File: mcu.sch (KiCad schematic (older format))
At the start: 53 parts, among them P11 CONN_01X01, P16 CONN_01X01, P17 CONN_01X01, P21 CONN_01X01, P22 CONN_01X01, P23 CONN_01X01, P28 CONN_01X01, P29 CONN_01X01, P3 CONN_01X05, P30 CONN_01X01, P32 CONN_01X01, P33 CONN_01X01, P34 CONN_01X01, P35 CONN_01X01, P36 CONN_01X01, P37 CONN_01X01, P4 CONN_01X04, P5 CONN_01X01, P6 CONN_01X01, P9 CONN_01X01, Y1 ABMM2-8.000MHZ-E2-T

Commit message: Stand 10.03
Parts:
- removed C37, C38: 18p, Capacitors_SMD:C_0603, symbol C_Small
- removed C40, C41: 1u, Capacitors_SMD:C_0603, symbol C_Small
- removed C44: 47u, Capacitors_SMD:C_0805, symbol C_Small
- removed C95: 100n, Capacitors_SMD:C_0603, symbol C_Small
- removed C960: 10u, Capacitors_SMD:C_0603, symbol C_Small
- removed D14: BAT54SW, TO_SOT_Packages_SMD:SOT-323, symbol BAT54SW
- removed Y1: ABMM2-8.000MHZ-E2-T, Crystals:Crystal_SMD_5032_4Pads, symbol Crystal_Small
- added C? (x2): 18p, symbol C_Small
- added P?: CONN_01X04, Connectors_Molex:Molex_KK-6410-04_04x2.54mm_Straight, symbol CONN_01X04
- added P? (x3): CONN_01X01, Connect:PINTST, symbol CONN_01X01
- added R? (x2): 10k, symbol R_Small
- added Y?: ABMM2-8.000MHZ-E2-T, Crystals:Crystal_SMD_5032-4pin_5.0x3.2mm, symbol Crystal_Small
- U?: value MKE14F256_v.1.1 -> MKE14F256_v.1.2; footprint (none) -> Housings_QFP:LQFP-64_10x10mm_Pitch0.5mm; symbol MKE14F256_v.1.1 -> MKE14F256_v.1.3
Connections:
- net labels added: DC_3V6, DC_Vin, PWM_HS, PWM_LS, led_blu
- net labels removed: ADC_CH_SEL, ADC_DVDD, PWM_HS_1, PWM_HS_2, PWM_HS_3, PWM_HS_4, PWM_LS_1, PWM_LS_2, PWM_LS_3, PWM_LS_4, Sense_Curr_1, Sense_Curr_2, Sense_Curr_3, Sense_Curr_4, Sense_Inp_Volt, Sense_Out_Volt_1, Sense_Out_Volt_2, Sense_Out_Volt_3, Sense_Out_Volt_4, VREFH, V_12V, led_ble
- wire segments 154 -> 131
- no-connect marks 5 -> 2
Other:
- moved on the sheet: P11, P16, P17, P21, P22, P23, P28, P29, P30, P9

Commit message: schematics ==> Check (exept BW) Layout started
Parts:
- added C37: 10n, Capacitors_SMD:C_0603, symbol C_Small
- C27, C28, C29, C30, C31, C32, C36: renamed from C?; footprint (none) -> Capacitors_SMD:C_0603
- C34: renamed from C?; value 100n -> 1n; footprint (none) -> Capacitors_SMD:C_0603
- D7: renamed from D15; footprint TO_SOT_Packages_SMD:SOT-323 -> TO_SOT_Packages_SMD:SOT-323_SC-70
- D8: renamed from D16; footprint TO_SOT_Packages_SMD:SOT-323 -> TO_SOT_Packages_SMD:SOT-323_SC-70
- R23, R24, R28: renamed from R?; footprint (none) -> Resistors_SMD:R_0603
- R25: renamed from R?; value 10k -> 47k; footprint (none) -> Resistors_SMD:R_0603
- XS1: renamed from XS?; footprint Connectors:Conn_uSDcard -> .pretty:uSDcard
- gave numbers to parts that had none: 6
- renumbered C501 to C33, C500 to C35, D5 to D3, D11 to D4, D13 to D5, D30 to D6, P30 to P10, P16 to P11, P11 to P12, P17 to P13, P21 to P14, P22 to P16, P23 to P17, P5 to P20, P6 to P21, P32 to P22, P33 to P23, P34 to P24, P35 to P25, P36 to P26, P37 to P27, P3 to P5, P4 to P6, P9 to P7, P28 to P8, P29 to P9, R36 to R19, R37 to R20, R38 to R21, R39 to R22, R49 to R26, R50 to R27
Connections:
- net GND: now also C37.1
- net Vref: now also C37.2
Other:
- moved on the sheet: C34

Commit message: changed usd slot
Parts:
- XS1: footprint .pretty:uSDcard -> .pretty:HIROSE-MICROSD-DM3AT-SF
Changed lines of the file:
@@
 F 0 "XS1" H 6330 9780 50  0000 C CNN
 F 1 "SD_ebay-uSD-push/push_SMD" V 5780 10355 50  0000 C CNN
-F 2 ".pretty:uSDcard" H 6105 10355 10  0001 C CNN
+F 2 ".pretty:HIROSE-MICROSD-DM3AT-SF" H 6105 10355 10  0001 C CNN
 F 3 "_" H 6105 10355 10  0001 C CNN
 F 4 "_" H 6105 10355 10  0001 C CNN "Manf#"

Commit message: All parts in places (exept :Leds)
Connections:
- net ADC_1: now also U7.52 (PTC6); no longer U7.51 (PTC7)
- net ADC_2: now also U7.54 (PTE2); no longer U7.52 (PTC6)
- net ADC_3: now also U7.51 (PTC7); no longer U7.53 (PTE6)
- net ADC_4: now also U7.53 (PTE6); no longer U7.54 (PTE2)
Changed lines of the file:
@@
 ADC_PDEN
 Text GLabel 10960 3460 2    39   Input ~ 0
+ADC_3
+Text GLabel 10960 3610 2    39   Input ~ 0
 ADC_1
-Text GLabel 10960 3610 2    39   Input ~ 0
+Text GLabel 10960 3760 2    39   Input ~ 0
+ADC_4
+Text GLabel 10960 3910 2    39   Input ~ 0
 ADC_2
-Text GLabel 10960 3760 2    39   Input ~ 0
-ADC_3
-Text GLabel 10960 3910 2    39   Input ~ 0
-ADC_4
 Text GLabel 3780 6060 0    60   Input ~ 0
 Boost_Enable

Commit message: Started with tracking
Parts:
- Y1: symbol Crystal_Small -> QUARTZCMS4
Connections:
- net at C28.1, U7.12 (PTB6): now also Y1.3; no longer Y1.2
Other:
- moved on the sheet: C27, C28
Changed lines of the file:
@@
 L C_Small C28
 U 1 1 58C580AB
-P 3455 7285
-F 0 "C28" H 3465 7355 50  0000 L CNN
-F 1 "18p" H 3465 7205 50  0000 L CNN
-F 2 "Capacitors_SMD:C_0603" H 3455 7285 50  0001 C CNN
-F 3 "" H 3455 7285 50  0000 C CNN
-	1    3455 7285
+P 3455 7210
+F 0 "C28" H 3465 7280 50  0000 L CNN
+F 1 "18p" H 3465 7130 50  0000 L CNN
+F 2 "Capacitors_SMD:C_0603" H 3455 7210 50  0001 C CNN
+F 3 "" H 3455 7210 50  0000 C CNN
+	1    3455 7210
 	1    0    0    -1
 $EndComp
@@
 L C_Small C27
 U 1 1 58C58C12
-P 3105 7280
-F 0 "C27" H 3115 7350 50  0000 L CNN
-F 1 "18p" H 3115 7200 50  0000 L CNN
-F 2 "Capacitors_SMD:C_0603" H 3105 7280 50  0001 C CNN
-F 3 "" H 3105 7280 50  0000 C CNN
-	1    3105 7280
-	1    0    0    -1
-$EndComp
-$Comp
-L Crystal_Small Y1
+P 2850 7200
+F 0 "C27" H 2860 7270 50  0000 L CNN
+F 1 "18p" H 2860 7120 50  0000 L CNN
+F 2 "Capacitors_SMD:C_0603" H 2850 7200 50  0001 C CNN
+F 3 "" H 2850 7200 50  0000 C CNN
+	1    2850 7200
+	1    0    0    -1
+$EndComp
+$Comp
+L QUARTZCMS4 Y1
 U 1 1 58C5C5B8
-P 3295 7045
-F 0 "Y1" H 3295 7145 50  0000 C CNN
-F 1 "ABMM2-8.000MHZ-E2-T" H 2600 7135 50  0000 C CNN
-F 2 "Crystals:Crystal_SMD_5032-4pin_5.0x3.2mm" H 3295 7045 50  0001 C CNN
-F 3 "http://www.mouser.com/ds/2/3/ABMM2-40161.pdf" H 3295 7045 50  0001 C CNN
-F 4 "815-ABMM2-8-E2T" H 3295 7045 60  0001 C CNN "Mouser"
-	1    3295 7045
+P 3150 7015
+F 0 "Y1" H 3150 7115 50  0000 C CNN
+F 1 "ABMM2-8.000MHZ-E2-T" H 2455 7105 50  0000 C CNN
+F 2 "Crystals:Crystal_SMD_5032-4pin_5.0x3.2mm" H 3150 7015 50  0001 C CNN
+F 3 "http://www.mouser.com/ds/2/3/ABMM2-40161.pdf" H 3150 7015 50  0001 C CNN
+F 4 "815-ABMM2-8-E2T" H 3150 7015 60  0001 C CNN "Mouser"
+	1    3150 7015
 	1    0    0    -1
 $EndComp
@@
 L GND #PWR075
 U 1 1 58C5EAC8
-P 3105 7415
-F 0 "#PWR075" H 3105 7165 50  0001 C CNN
-F 1 "GND" H 3105 7265 50  0000 C CNN
-F 2 "" H 3105 7415 50  0000 C CNN
-F 3 "" H 3105 7415 50  0000 C CNN
-	1    3105 7415
+P 2850 7340
+F 0 "#PWR075" H 2850 7090 50  0001 C CNN
+F 1 "GND" H 2850 7190 50  0000 C CNN
+F 2 "" H 2850 7340 50  0000 C CNN
+F 3 "" H 2850 7340 50  0000 C CNN
+	1    2850 7340
 	1    0    0    -1
 $EndComp
@@
 L GND #PWR076
 U 1 1 58C5F3E4
-P 3455 7415
-F 0 "#PWR076" H 3455 7165 50  0001 C CNN
-F 1 "GND" H 3455 7265 50  0000 C CNN
-F 2 "" H 3455 7415 50  0000 C CNN
-F 3 "" H 3455 7415 50  0000 C CNN
-	1    3455 7415
+P 3455 7340
+F 0 "#PWR076" H 3455 7090 50  0001 C CNN
+F 1 "GND" H 3455 7190 50  0000 C CNN
+F 2 "" H 3455 7340 50  0000 C CNN
+F 3 "" H 3455 7340 50  0000 C CNN
+	1    3455 7340
 	1    0    0    -1
 $EndComp
@@
 Wire Wire Line
 	10960 3910 10825 3910
-Connection ~ 3105 7045
-Wire Wire Line
-	3925 6710 3105 6710
-Connection ~ 3455 7045
+Wire Wire Line
+	2850 6710 3925 6710
 Wire Wire Line
 	3925 6860 3455 6860
 Wire Wire Line
-	3455 7415 3455 7385
-Wire Wire Line
-	3105 7415 3105 7380
-Wire Wire Line
-	3105 6710 3105 7180
-Wire Wire Line
-	3195 7045 3105 7045
-Wire Wire Line
-	3455 7045 3395 7045
-Wire Wire Line
-	3455 6860 3455 7185
+	3455 7340 3455 7310
+Wire Wire Line
+	2850 7340 2850 7300
 Wire Wire Line
 	11070 6210 10825 6210
@@
 $EndComp
 Wire Wire Line
-	8990 1970 8740 1970
+	8740 1970 8990 1970
 Connection ~ 8875 1970
 Wire Wire Line
@@
 	8945 2135 8945 1970
 Connection ~ 8945 1970
+Wire Wire Line
+	3455 6860 3455 7110
+Wire Wire Line
+	3455 7015 3450 7015
+Connection ~ 3455 7015
+Wire Wire Line
+	2850 6710 2850 7100
+Connection ~ 2850 7015
 $EndSCHEMATC

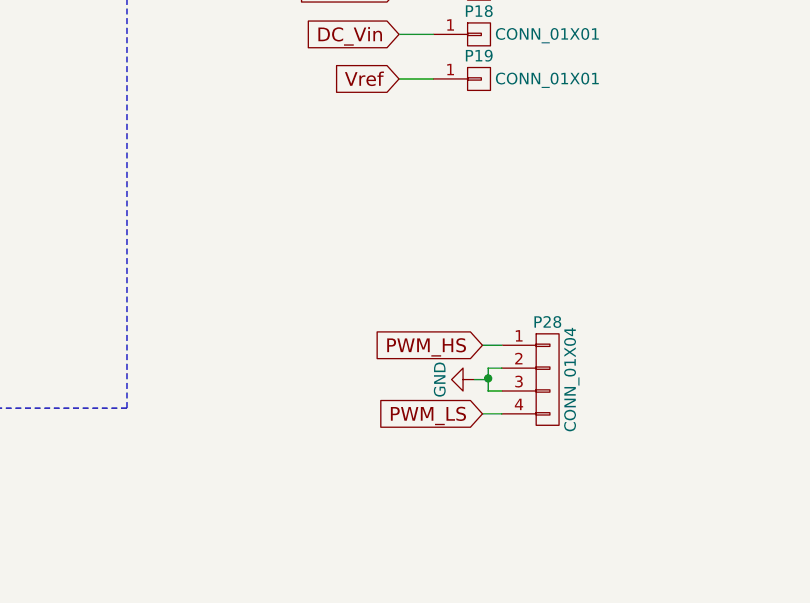
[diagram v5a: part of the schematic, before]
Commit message: added missing parts (SPI conn / Boost Conn/ drills..)
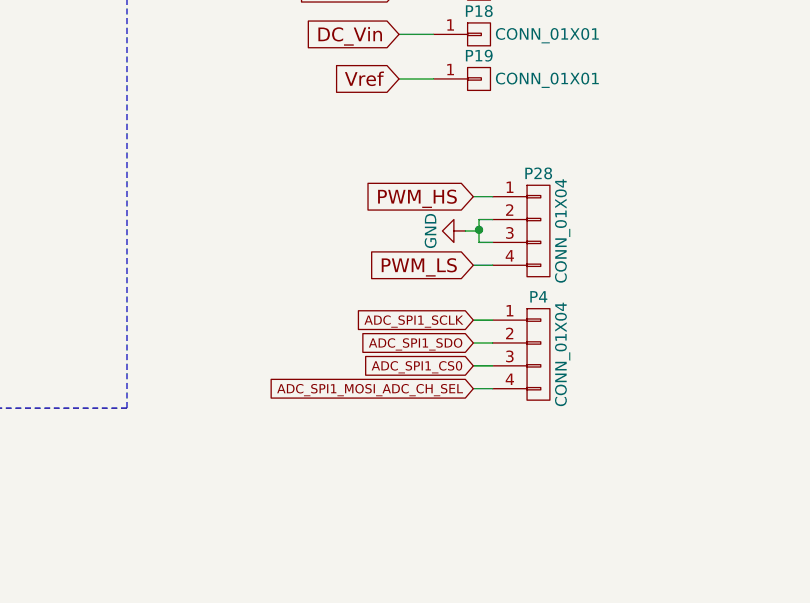
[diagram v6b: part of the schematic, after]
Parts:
- added P4: CONN_01X04, Connectors_Molex:Molex_KK-6410-04_04x2.54mm_Straight, symbol CONN_01X04
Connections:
- net ADC_SPI1_CS0: now also P4.3 (P3)
- net ADC_SPI1_MOSI_ADC_CH_SEL: now also P4.4 (P4)
- net ADC_SPI1_SCLK: now also P4.1 (P1)
- net ADC_SPI1_SDO: now also P4.2 (P2)
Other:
- moved on the sheet: P28

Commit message: still the regulators & Planes fill
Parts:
- U7: symbol MKE14F256_v.1.3 -> MKE14F256_v.1.4
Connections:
- net ADC_PDEN: now also U7.26 (PTC0); no longer U7.43 (PTB12)
- net led_blu: now also U7.47 (PTA3); no longer U7.28 (PTC16)
- net led_grn: now also U7.49 (PTA1); no longer U7.27 (PTC17)
- net led_red: now also U7.48 (PTA2); no longer U7.25 (PTC1)
- net led_yel: now also U7.50 (PTA0); no longer U7.26 (PTC0)
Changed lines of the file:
@@
 $EndComp
 $Comp
-L +3.3V #PWR71
+L +3.3V #PWR046
 U 1 1 57321F1B
 P 10876 9751
-F 0 "#PWR71" H 10876 9601 50  0001 C CNN
+F 0 "#PWR046" H 10876 9601 50  0001 C CNN
 F 1 "+3.3V" H 10876 9891 50  0000 C CNN
 F 2 "" H 10876 9751 50  0000 C CNN
@@
 $EndComp
 $Comp
-L GND #PWR72
+L GND #PWR047
 U 1 1 573220D0
 P 10876 10251
-F 0 "#PWR72" H 10876 10001 50  0001 C CNN
+F 0 "#PWR047" H 10876 10001 50  0001 C CNN
 F 1 "GND" H 10876 10101 50  0000 C CNN
 F 2 "" H 10876 10251 50  0000 C CNN
@@
 $EndComp
 $Comp
-L GND #PWR70
+L GND #PWR048
 U 1 1 57323943
 P 10176 10501
-F 0 "#PWR70" H 10176 10251 50  0001 C CNN
+F 0 "#PWR048" H 10176 10251 50  0001 C CNN
 F 1 "GND" H 10176 10351 50  0000 C CNN
 F 2 "" H 10176 10501 50  0000 C CNN
@@
 $EndComp
 $Comp
-L +3.3V #PWR64
+L +3.3V #PWR049
 U 1 1 57323984
 P 8976 10451
-F 0 "#PWR64" H 8976 10301 50  0001 C CNN
+F 0 "#PWR049" H 8976 10301 50  0001 C CNN
 F 1 "+3.3V" H 8976 10591 50  0000 C CNN
 F 2 "" H 8976 10451 50  0000 C CNN
@@
 $EndComp
 $Comp
-L +3.3V #PWR68
+L +3.3V #PWR050
 U 1 1 573239C5
 P 9626 10451
-F 0 "#PWR68" H 9626 10301 50  0001 C CNN
+F 0 "#PWR050" H 9626 10301 50  0001 C CNN
 F 1 "+3.3V" H 9626 10591 50  0000 C CNN
 F 2 "" H 9626 10451 50  0000 C CNN
@@
 $EndComp
 $Comp
-L GND #PWR67
+L GND #PWR051
 U 1 1 57323B3B
 P 9476 10501
-F 0 "#PWR67" H 9476 10251 50  0001 C CNN
+F 0 "#PWR051" H 9476 10251 50  0001 C CNN
 F 1 "GND" H 9476 10351 50  0000 C CNN
 F 2 "" H 9476 10501 50  0000 C CNN
@@
 $EndComp
 $Comp
-L +3.3V #PWR55
+L +3.3V #PWR052
 U 1 1 57346289
 P 4291 9953
-F 0 "#PWR55" H 4291 9803 50  0001 C CNN
+F 0 "#PWR052" H 4291 9803 50  0001 C CNN
 F 1 "+3.3V" H 4291 10093 50  0000 C CNN
 F 2 "" H 4291 9953 50  0000 C CNN
@@
 $EndComp
 $Comp
-L GND #PWR54
+L GND #PWR053
 U 1 1 57346821
 P 4241 10453
-F 0 "#PWR54" H 4241 10203 50  0001 C CNN
+F 0 "#PWR053" H 4241 10203 50  0001 C CNN
 F 1 "GND" H 4241 10303 50  0000 C CNN
 F 2 "" H 4241 10453 50  0000 C CNN
@@
 ADC_1
 $Comp
-L +3.3V #PWR75
+L +3.3V #PWR054
 U 1 1 57613741
 P 14935 5810
-F 0 "#PWR75" H 14935 5660 50  0001 C CNN
+F 0 "#PWR054" H 14935 5660 50  0001 C CNN
 F 1 "+3.3V" H 14935 5950 50  0000 C CNN
 F 2 "" H 14935 5810 50  0000 C CNN
@@
 $EndComp
 $Comp
-L GND #PWR77
+L GND #PWR055
 U 1 1 57613EB7
 P 14935 6310
-F 0 "#PWR77" H 14935 6060 50  0001 C CNN
+F 0 "#PWR055" H 14935 6060 50  0001 C CNN
 F 1 "GND" H 14935 6160 50  0000 C CNN
 F 2 "" H 14935 6310 50  0000 C CNN
@@
 $EndComp
 $Comp
-L GND #PWR78
+L GND #PWR056
 U 1 1 57614C38
 P 14935 6560
-F 0 "#PWR78" H 14935 6310 50  0001 C CNN
+F 0 "#PWR056" H 14935 6310 50  0001 C CNN
 F 1 "GND" H 14935 6410 50  0000 C CNN
 F 2 "" H 14935 6560 50  0000 C CNN
@@
 $EndComp
 $Comp
-L +3.3V #PWR80
+L +3.3V #PWR057
 U 1 1 57618324
 P 14940 6965
-F 0 "#PWR80" H 14940 6815 50  0001 C CNN
+F 0 "#PWR057" H 14940 6815 50  0001 C CNN
 F 1 "+3.3V" H 14940 7105 50  0000 C CNN
 F 2 "" H 14940 6965 50  0000 C CNN
@@
 $EndComp
 $Comp
-L GND #PWR46
+L GND #PWR058
 U 1 1 576344D4
 P 1622 10663
-F 0 "#PWR46" H 1622 10413 50  0001 C CNN
+F 0 "#PWR058" H 1622 10413 50  0001 C CNN
 F 1 "GND" H 1622 10513 50  0000 C CNN
 F 2 "" H 1622 10663 50  0000 C CNN
@@
 $EndComp
 $Comp
-L GND #PWR47
+L GND #PWR059
 U 1 1 57634A1E
 P 1972 10663
-F 0 "#PWR47" H 1972 10413 50  0001 C CNN
+F 0 "#PWR059" H 1972 10413 50  0001 C CNN
 F 1 "GND" H 1972 10513 50  0000 C CNN
 F 2 "" H 1972 10663 50  0000 C CNN
@@
 $EndComp
 $Comp
-L GND #PWR48
+L GND #PWR060
 U 1 1 57634A8E
 P 2272 10663
-F 0 "#PWR48" H 2272 10413 50  0001 C CNN
+F 0 "#PWR060" H 2272 10413 50  0001 C CNN
 F 1 "GND" H 2272 10513 50  0000 C CNN
 F 2 "" H 2272 10663 50  0000 C CNN
@@
 $EndComp
 $Comp
-L GND #PWR49
+L GND #PWR061
 U 1 1 57634AFE
 P 2572 10663
-F 0 "#PWR49" H 2572 10413 50  0001 C CNN
+F 0 "#PWR061" H 2572 10413 50  0001 C CNN
 F 1 "GND" H 2572 10513 50  0000 C CNN
 F 2 "" H 2572 10663 50  0000 C CNN
@@
 CMP1_IN1_Overvoltage_Prot
 $Comp
-L GND #PWR76
+L GND #PWR062
 U 1 1 57C00D54
 P 14935 6060
-F 0 "#PWR76" H 14935 5810 50  0001 C CNN
+F 0 "#PWR062" H 14935 5810 50  0001 C CNN
 F 1 "GND" H 14935 5910 50  0000 C CNN
 F 2 "" H 14935 6060 50  0000 C CNN
@@
 $EndComp
 $Comp
-L GND #PWR69
+L GND #PWR063
 U 1 1 57C35C43
 P 9656 10791
-F 0 "#PWR69" H 9656 10541 50  0001 C CNN
+F 0 "#PWR063" H 9656 10541 50  0001 C CNN
 F 1 "GND" H 9656 10641 50  0000 C CNN
 F 2 "" H 9656 10791 50  0000 C CNN
@@
 $EndComp
 $Comp
-L GND #PWR65
+L GND #PWR064
 U 1 1 57C35CF6
 P 9006 10791
-F 0 "#PWR65" H 9006 10541 50  0001 C CNN
+F 0 "#PWR064" H 9006 10541 50  0001 C CNN
 F 1 "GND" H 9006 10641 50  0000 C CNN
 F 2 "" H 9006 10791 50  0000 C CNN
@@
 $EndComp
 $Comp
-L +3.3V #PWR56
+L +3.3V #PWR065
 U 1 1 58BE06E5
 P 5955 9380
-F 0 "#PWR56" H 5955 9230 50  0001 C CNN
+F 0 "#PWR065" H 5955 9230 50  0001 C CNN
 F 1 "+3.3V" H 5955 9520 50  0000 C CNN
 F 2 "" H 5955 9380 50  0000 C CNN
@@
 $EndComp
 $Comp
-L GND #PWR58
+L GND #PWR066
 U 1 1 58BE131B
 P 6240 9645
-F 0 "#PWR58" H 6240 9395 50  0001 C CNN
+F 0 "#PWR066" H 6240 9395 50  0001 C CNN
 F 1 "GND" H 6240 9495 50  0000 C CNN
 F 2 "" H 6240 9645 50  0000 C CNN
@@
 $EndComp
 $Comp
-L GND #PWR57
+L GND #PWR067
 U 1 1 58BE2C3C
 P 5955 11020
-F 0 "#PWR57" H 5955 10770 50  0001 C CNN
+F 0 "#PWR067" H 5955 10770 50  0001 C CNN
 F 1 "GND" H 5955 10870 50  0000 C CNN
 F 2 "" H 5955 11020 50  0000 C CNN
@@
 Text GLabel 11070 6060 2    60   Input ~ 0
 ADC_SPI1_CS0
-Text GLabel 11060 2560 2    60   Input ~ 0
+Text GLabel 3690 3410 0    60   Input ~ 0
 ADC_PDEN
 Text GLabel 10960 3460 2    39   Input ~ 0
@@
 Vref
 $Comp
-L +3.3V #PWR61
+L +3.3V #PWR068
 U 1 1 58C38171
 P 8075 1195
-F 0 "#PWR61" H 8075 1045 50  0001 C CNN
+F 0 "#PWR068" H 8075 1045 50  0001 C CNN
 F 1 "+3.3V" H 8075 1335 50  0000 C CNN
 F 2 "" H 8075 1195 50  0000 C CNN
@@
 $EndComp
 $Comp
-L +3.3V #PWR62
+L +3.3V #PWR069
 U 1 1 58C38898
 P 8275 1190
-F 0 "#PWR62" H 8275 1040 50  0001 C CNN
+F 0 "#PWR069" H 8275 1040 50  0001 C CNN
 F 1 "+3.3V" H 8275 1330 50  0000 C CNN
 F 2 "" H 8275 1190 50  0000 C CNN
@@
 $EndComp
 $Comp
-L +3.3V #PWR63
+L +3.3V #PWR070
 U 1 1 58C38936
 P 8475 1190
-F 0 "#PWR63" H 8475 1040 50  0001 C CNN
+F 0 "#PWR070" H 8475 1040 50  0001 C CNN
 F 1 "+3.3V" H 8475 1330 50  0000 C CNN
 F 2 "" H 8475 1190 50  0000 C CNN
@@
 $EndComp
 $Comp
-L GND #PWR66
+L GND #PWR071
 U 1 1 58C3DCC7
 P 9365 2030
-F 0 "#PWR66" H 9365 1780 50  0001 C CNN
+F 0 "#PWR071" H 9365 1780 50  0001 C CNN
 F 1 "GND" H 9365 1880 50  0000 C CNN
 F 2 "" H 9365 2030 50  0000 C CNN
@@
 $EndComp
 $Comp
-L GND #PWR60
+L GND #PWR072
 U 1 1 58C4F8DB
 P 6475 7740
-F 0 "#PWR60" H 6475 7490 50  0001 C CNN
+F 0 "#PWR072" H 6475 7490 50  0001 C CNN
 F 1 "GND" H 6475 7590 50  0000 C CNN
 F 2 "" H 6475 7740 50  0000 C CNN
@@
 $EndComp
 $Comp
-L GND #PWR59
+L GND #PWR073
 U 1 1 58C4FCDC
 P 6275 7740
-F 0 "#PWR59" H 6275 7490 50  0001 C CNN
+F 0 "#PWR073" H 6275 7490 50  0001 C CNN
 F 1 "GND" H 6275 7590 50  0000 C CNN
 F 2 "" H 6275 7740 50  0000 C CNN
@@
 $EndComp
 $Comp
-L +3.3V #PWR74
+L +3.3V #PWR074
 U 1 1 58C66D72
 P 11680 7160
-F 0 "#PWR74" H 11680 7010 50  0001 C CNN
+F 0 "#PWR074" H 11680 7010 50  0001 C CNN
 F 1 "+3.3V" H 11680 7300 50  0000 C CNN
 F 2 "" H 11680 7160 50  0000 C CNN
@@
 $EndComp
 $Comp
-L GND #PWR73
+L GND #PWR075
 U 1 1 58C68B69
 P 11240 7505
-F 0 "#PWR73" H 11240 7255 50  0001 C CNN
+F 0 "#PWR075" H 11240 7255 50  0001 C CNN
 F 1 "GND" H 11240 7355 50  0000 C CNN
 F 2 "" H 11240 7505 50  0000 C CNN
@@
 $EndComp
 $Comp
-L GND #PWR50
+L GND #PWR076
 U 1 1 58C5EAC8
 P 2850 7340
-F 0 "#PWR50" H 2850 7090 50  0001 C CNN
+F 0 "#PWR076" H 2850 7090 50  0001 C CNN
 F 1 "GND" H 2850 7190 50  0000 C CNN
 F 2 "" H 2850 7340 50  0000 C CNN
@@
 $EndComp
 $Comp
-L GND #PWR51
+L GND #PWR077
 U 1 1 58C5F3E4
 P 3455 7340
-F 0 "#PWR51" H 3455 7090 50  0001 C CNN
+F 0 "#PWR077" H 3455 7090 50  0001 C CNN
 F 1 "GND" H 3455 7190 50  0000 C CNN
 F 2 "" H 3455 7340 50  0000 C CNN
@@
 $EndComp
 $Comp
-L GND #PWR52
+L GND #PWR078
 U 1 1 58C97D80
 P 3465 2975
-F 0 "#PWR52" H 3465 2725 50  0001 C CNN
+F 0 "#PWR078" H 3465 2725 50  0001 C CNN
 F 1 "GND" H 3465 2825 50  0000 C CNN
 F 2 "" H 3465 2975 50  0000 C CNN
@@
 $EndComp
 $Comp
-L GND #PWR53
+L GND #PWR079
 U 1 1 58C9831F
 P 3675 2975
-F 0 "#PWR53" H 3675 2725 50  0001 C CNN
+F 0 "#PWR079" H 3675 2725 50  0001 C CNN
 F 1 "GND" H 3675 2825 50  0000 C CNN
 F 2 "" H 3675 2975 50  0000 C CNN
@@
 	15250 8375 15165 8375
 $Comp
-L GND #PWR81
+L GND #PWR080
 U 1 1 58CA8BCD
 P 15130 8225
-F 0 "#PWR81" H 15130 7975 50  0001 C CNN
+F 0 "#PWR080" H 15130 7975 50  0001 C CNN
 F 1 "GND" H 15130 8075 50  0000 C CNN
 F 2 "" H 15130 8225 50  0000 C CNN
@@
 $EndComp
 $Comp
-L GND #PWR79
+L GND #PWR081
 U 1 1 58CC57BD
 P 14940 6755
-F 0 "#PWR79" H 14940 6505 50  0001 C CNN
+F 0 "#PWR081" H 14940 6505 50  0001 C CNN
 F 1 "GND" H 14940 6605 50  0000 C CNN
 F 2 "" H 14940 6755 50  0000 C CNN
@@
 Wire Wire Line
 	14940 6755 14990 6755
-Text GLabel 3495 3260 0    50   Input ~ 0
+Text GLabel 11255 3310 2    50   Input ~ 0
+led_yel
+Text GLabel 11265 3160 2    50   Input ~ 0
+led_grn
+Text GLabel 11255 3010 2    50   Input ~ 0
 led_red
-Text GLabel 3485 3410 0    50   Input ~ 0
-led_yel
-Text GLabel 3495 3560 0    50   Input ~ 0
-led_grn
-Text GLabel 3490 3710 0    50   Input ~ 0
+Text GLabel 11260 2860 2    50   Input ~ 0
 led_blu
 Wire Wire Line
-	3925 3560 3495 3560
-Wire Wire Line
-	3485 3410 3925 3410
-Wire Wire Line
-	3490 3710 3925 3710
-Wire Wire Line
-	3495 3260 3925 3260
-Wire Wire Line
-	11060 2560 10825 2560
+	10825 3010 11255 3010
+Wire Wire Line
+	11265 3160 10825 3160
+Wire Wire Line
+	11260 2860 10825 2860
+Wire Wire Line
+	11255 3310 10825 3310
+Wire Wire Line
+	3690 3410 3925 3410
 Wire Wire Line
 	3780 6060 3925 6060
 $Comp
-L MKE14F256_v.1.3 U7
+L MKE14F256_v.1.4 U7
 U 1 1 58C84028
 P 7075 4810

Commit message: connected Boost. Still inner layers
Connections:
- net PWM_HS: now also P28.4 (P4); no longer P28.1 (P1)
- net PWM_LS: now also P28.1 (P1); no longer P28.4 (P4)
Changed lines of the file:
@@
 PWM_LS
 Text GLabel 15165 8075 0    60   Input ~ 0
+PWM_LS
+Text GLabel 15165 8375 0    60   Input ~ 0
 PWM_HS
-Text GLabel 15165 8375 0    60   Input ~ 0
-PWM_LS
 $Comp
 L CONN_01X04 P28
